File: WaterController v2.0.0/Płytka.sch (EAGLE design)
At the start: 13 parts, among them IC1 DS1307ZN+, Q1 AOD2922, Q2 AOD2922

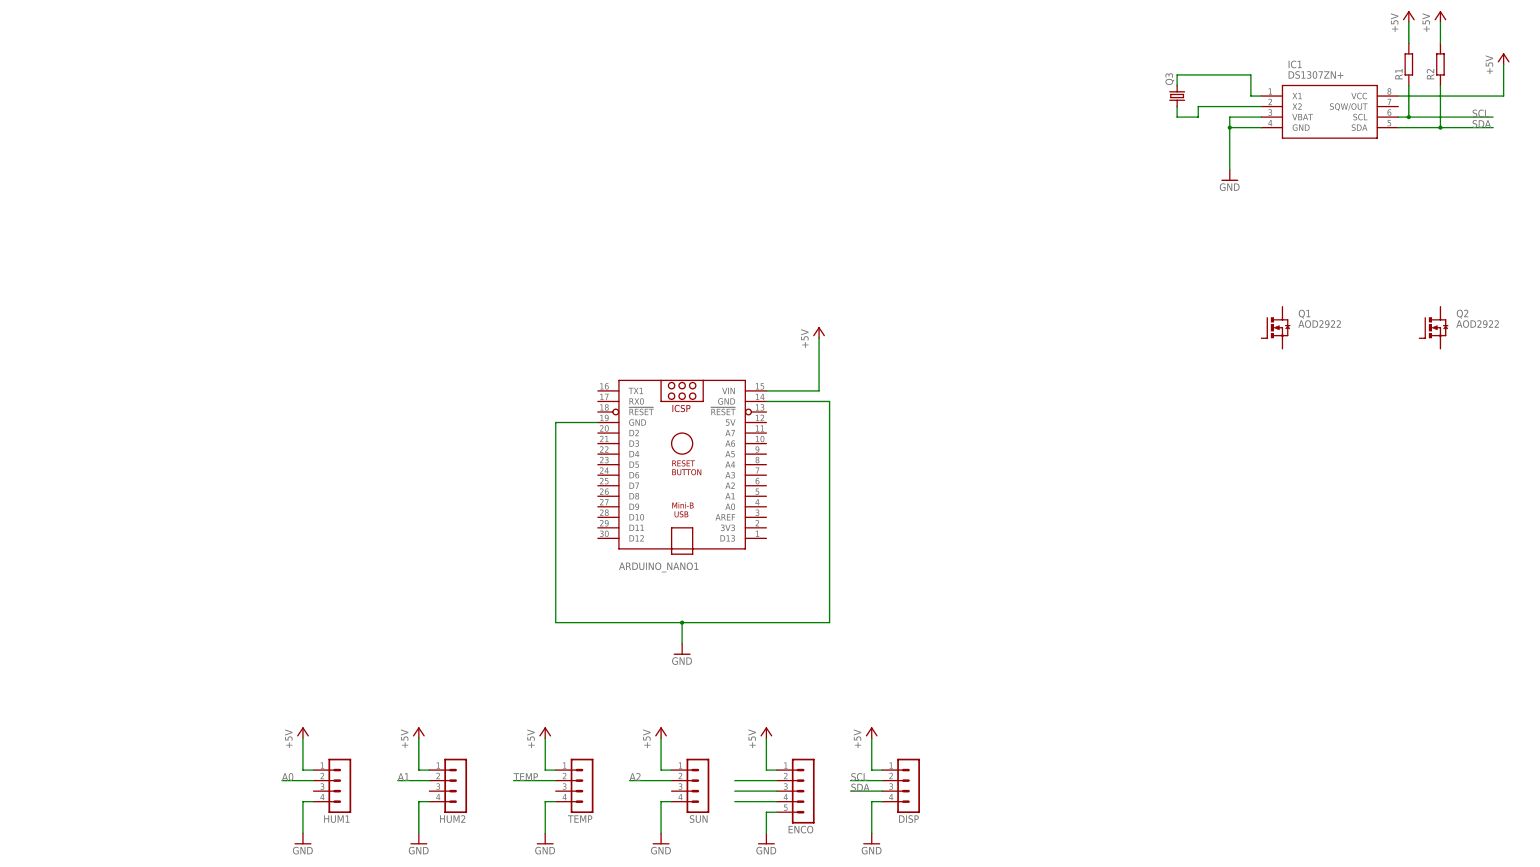
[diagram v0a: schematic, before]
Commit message: End schematic in eagle
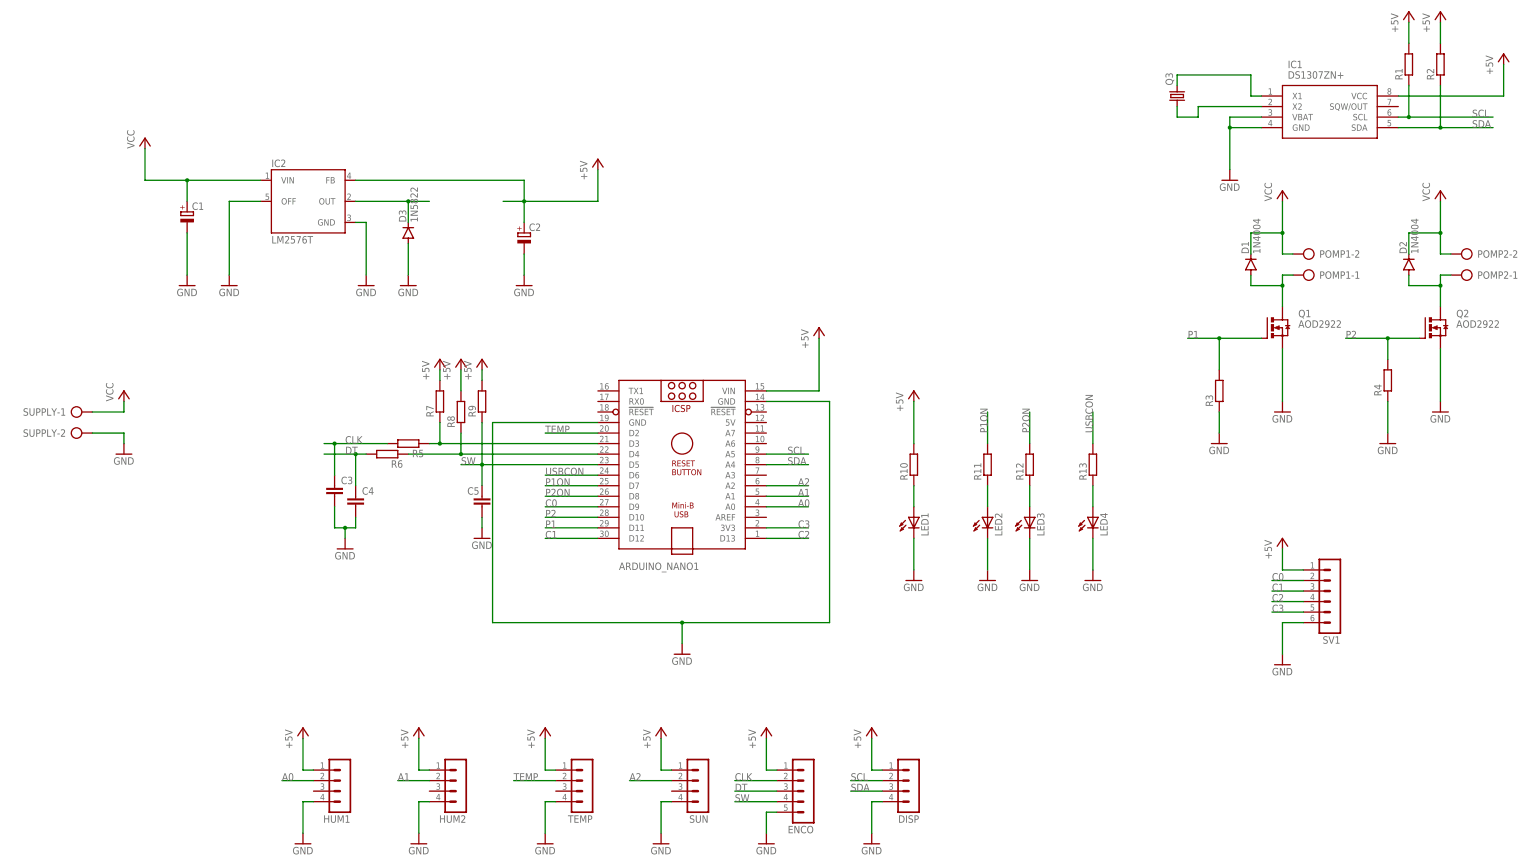
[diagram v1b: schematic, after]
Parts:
- added C1, C2: (no value), rcl:CPOL-EUE2.5-6
- added C3, C4, C5: (no value), capacitor-wima:C2,5-3
- added D1, D2: 1N4004, diode:1N4004
- added D3: 1N5822, diode:1N4004
- added IC2: LM2576T, v-reg-3:LM2576T
- added LED1, LED2, LED3, LED4: (no value), eagle-ltspice:LED_ELD260
- added POMP1, POMP2, SUPPLY: (no value), con-ptr500:AK500/2-H
- added R10, R11, R12, R13, R3, R4, R5, R6, R7, R8, R9: (no value), rcl:R-EU_R0805
- added SV1: (no value), con-lstb:MA06-1
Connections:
- removed net N$9: ENCO.4
- new net C0: ARDUINO_NANO1.D9, SV1.2
- new net C1: ARDUINO_NANO1.D12, SV1.3
- new net C2: ARDUINO_NANO1.D13, SV1.4
- new net C3: ARDUINO_NANO1.3V3, SV1.5
- new net CLK: C3.1, ENCO.2, R5.2
- new net DT: C4.1, ENCO.3, R6.2
- new net N$1: ARDUINO_NANO1.D3, R5.1, R7.1
- new net N$12: D1.A, POMP1-1.KL, Q1.D
- new net N$13: D2.A, POMP2-1.KL, Q2.D
- new net N$19: D3.C, IC2.OUT
- new net N$2: ARDUINO_NANO1.D4, R6.1, R8.1
- new net N$3: LED1.A, R10.1
- new net N$7: LED4.A, R13.1
- new net P1: ARDUINO_NANO1.D11, Q1.G, R3.2
- new net P1ON: ARDUINO_NANO1.D7, R11.2
- new net P2: ARDUINO_NANO1.D10, Q2.G, R4.2
- new net P2ON: ARDUINO_NANO1.D8, R12.2
- new net SW: ARDUINO_NANO1.D5, C5.1, ENCO.4, R9.1
- new net USBCON: ARDUINO_NANO1.D6, R13.2
- new net VCC: C1.+, D1.C, D2.C, IC2.VIN, POMP1-2.KL, POMP2-2.KL, SUPPLY-1.KL
- net +5V: now also C2.+, IC2.FB, R10.2, R7.2, R8.2, R9.2, SV1.1
- net A0: now also ARDUINO_NANO1.A0
- net A1: now also ARDUINO_NANO1.A1
- net A2: now also ARDUINO_NANO1.A2
- net GND: now also C1.-, C2.-, C3.2, C4.2, C5.2, D3.A, IC2.GND, IC2.OFF, LED1.C, LED2.C, LED3.C, LED4.C, Q1.S, Q2.S, R3.1, R4.1, SUPPLY-2.KL, SV1.6
- net N$5: now also LED2.A, R11.1; no longer ENCO.2
- net N$6: now also LED3.A, R12.1; no longer ENCO.3
- net SCL: now also ARDUINO_NANO1.A5
- net SDA: now also ARDUINO_NANO1.A4
- net TEMP: now also ARDUINO_NANO1.D2

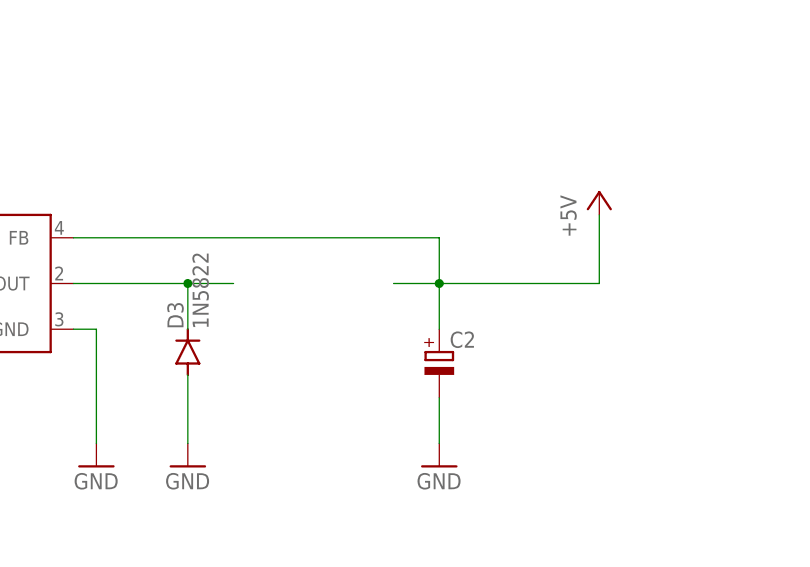
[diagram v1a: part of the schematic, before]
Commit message: Add new items in PCB
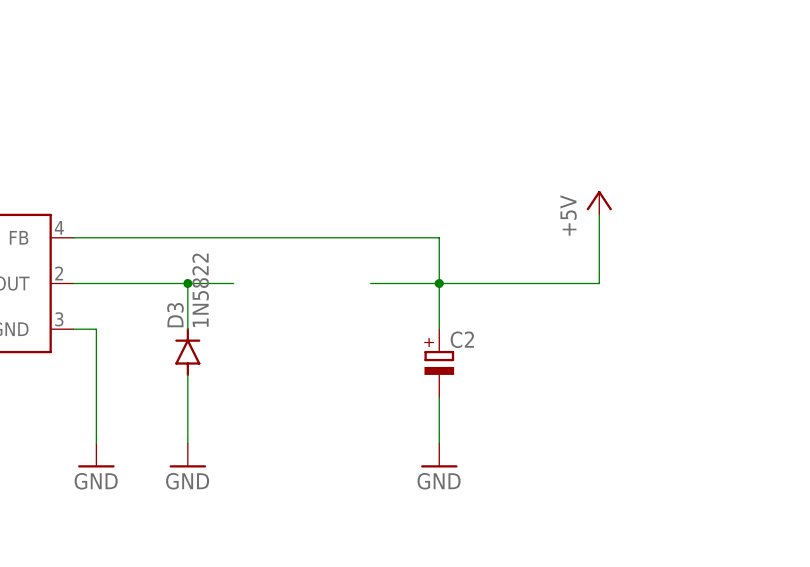
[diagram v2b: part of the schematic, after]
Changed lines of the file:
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@@
 <pinref part="C2" gate="G$1" pin="+"/>
 <wire x1="5.08" y1="162.56" x2="5.08" y2="167.64" width="0.1524" layer="91"/>
-<wire x1="5.08" y1="167.64" x2="0" y2="167.64" width="0.1524" layer="91"/>
+<wire x1="5.08" y1="167.64" x2="-2.54" y2="167.64" width="0.1524" layer="91"/>
 <pinref part="IC2" gate="A" pin="FB"/>
 <wire x1="-35.56" y1="172.72" x2="5.08" y2="172.72" width="0.1524" layer="91"/>
